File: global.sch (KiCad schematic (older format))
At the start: 37 parts, among them Q5 MMBT3904, U11 74HC165, U12 74HC595, U13 74HC595, U14 74HC595, U5 74HCT125

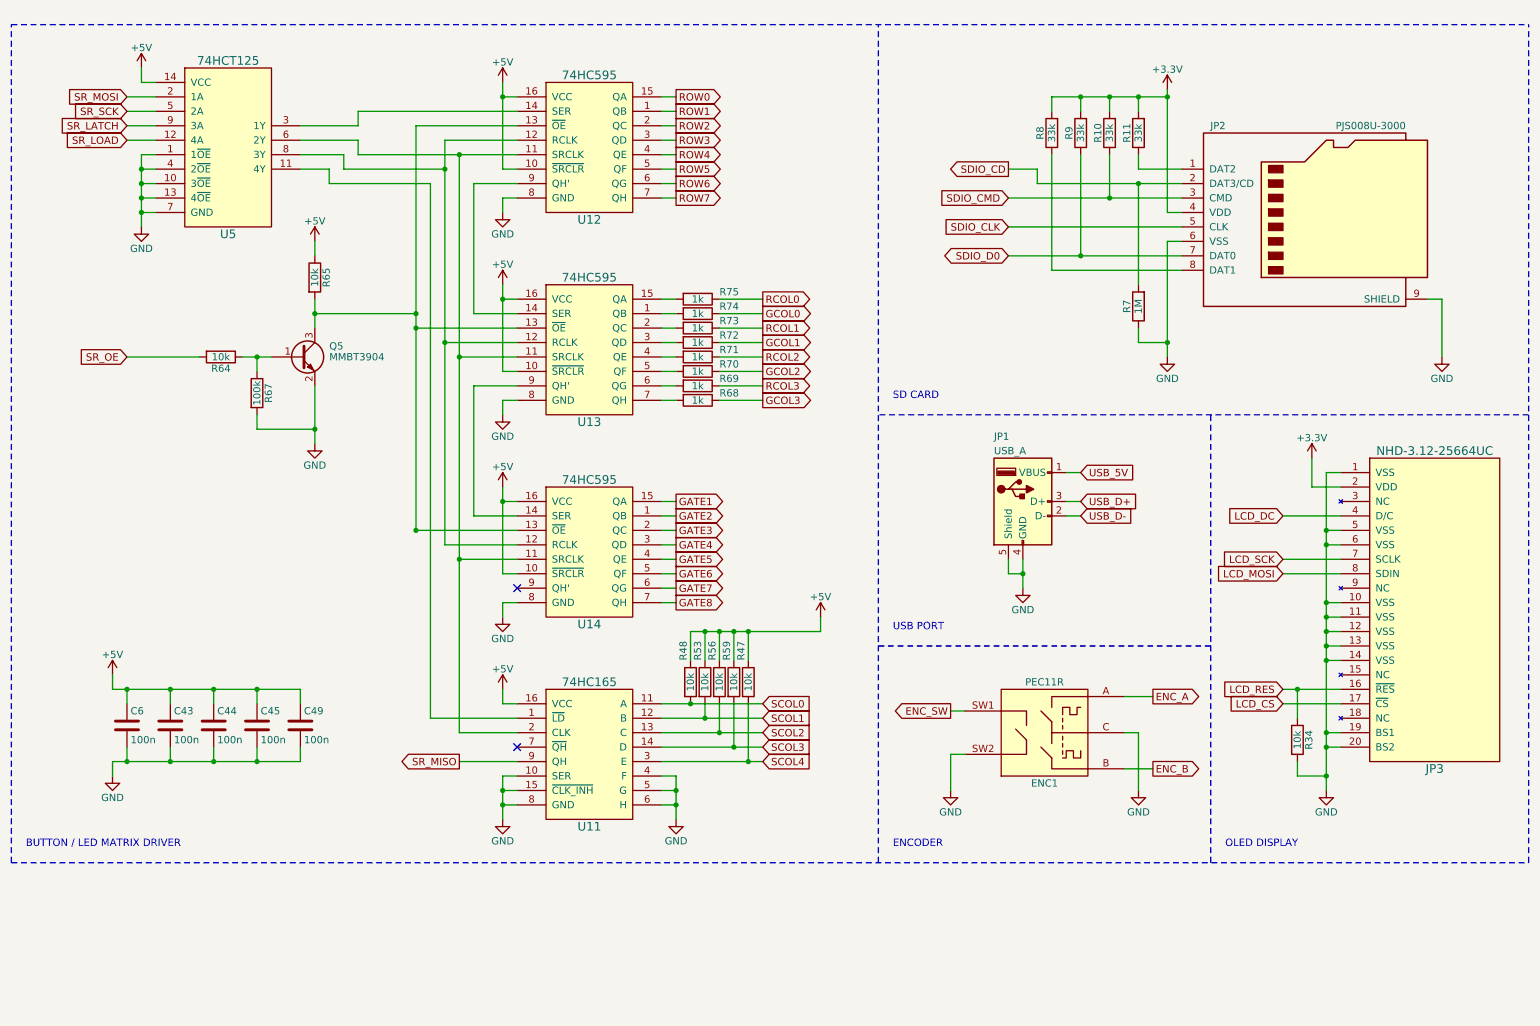
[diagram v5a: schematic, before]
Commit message: revised schematic and pcb
- fixed clock/reset inputs
- schematic annotations
- moved to cc-by-nc-sa
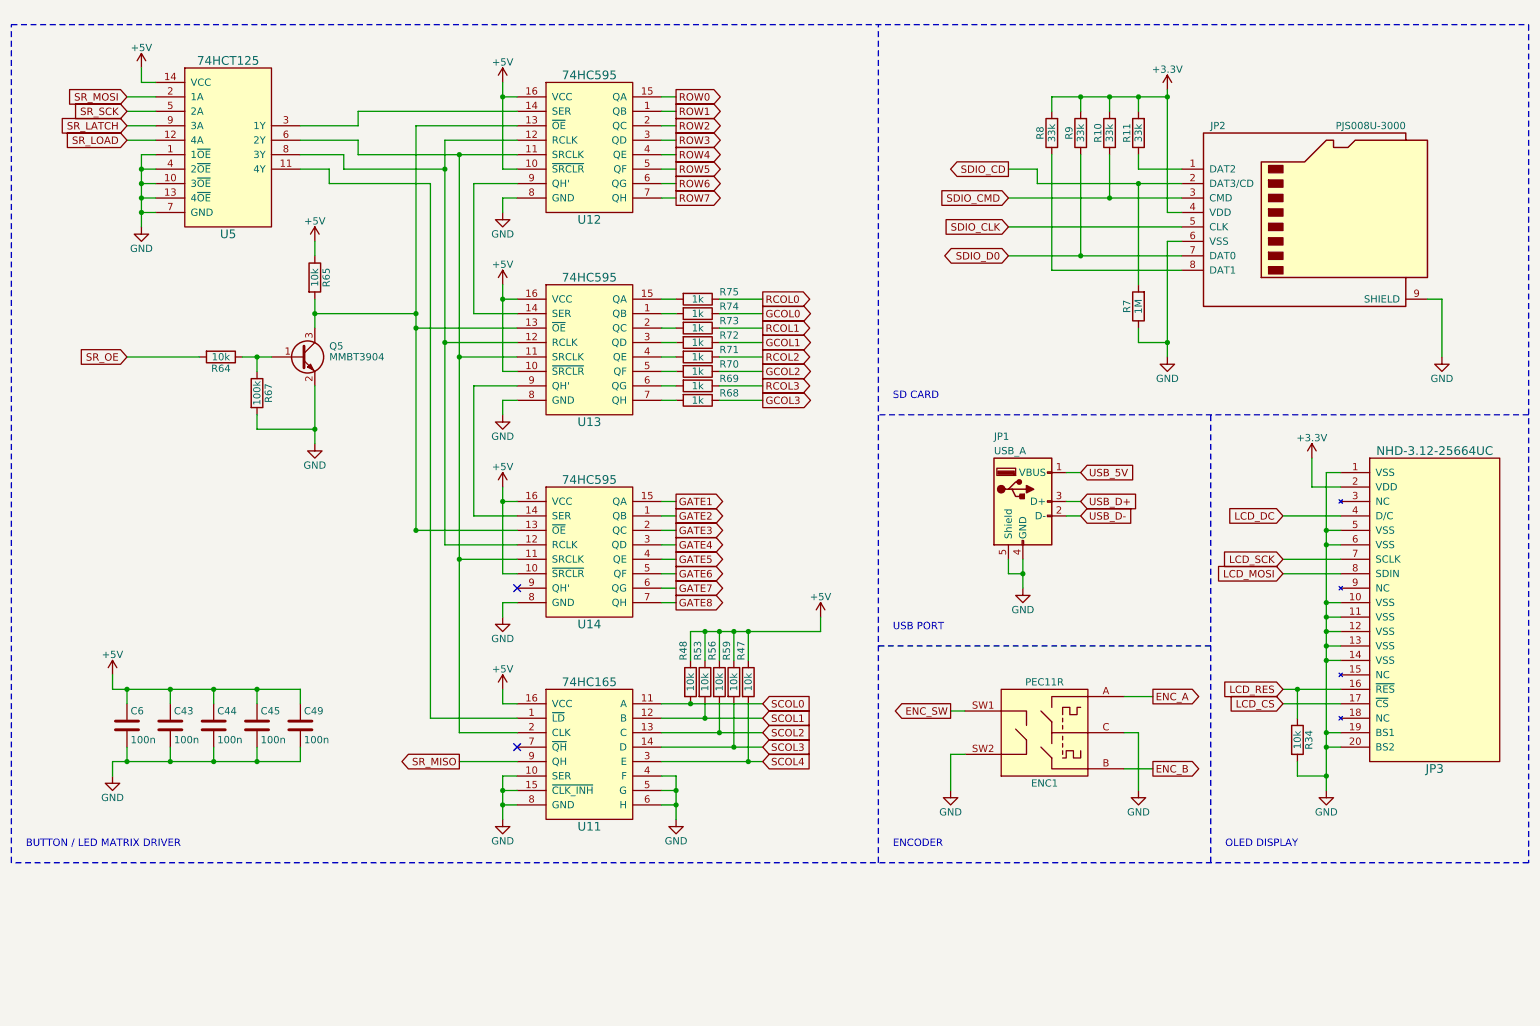
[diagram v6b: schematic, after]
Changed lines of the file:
@@
 Text GLabel 1400 2900 0    51   Input ~ 0
 SR_OE
+Text Notes 700  6300 0    51   ~ 0
+BUTTON / LED MATRIX DRIVER
+Text Notes 6700 3200 0    51   ~ 0
+SD CARD
+Text Notes 9000 6300 0    51   ~ 0
+OLED DISPLAY
+Text Notes 6700 6300 0    51   ~ 0
+ENCODER
+Text Notes 6700 4800 0    51   ~ 0
+USB PORT
 Wire Wire Line
 	5100 1100 5200 1100
@@
 Wire Wire Line
 	2300 3400 2700 3400
+Wire Notes Line
+	600  600  11100 600
+Wire Notes Line
+	11100 600  11100 6400
+Wire Notes Line
+	11100 3300 6600 3300
+Wire Notes Line
+	11100 6400 600  6400
+Wire Notes Line
+	8900 6400 8900 3300
+Wire Notes Line
+	8900 4900 6600 4900
+Wire Notes Line
+	6600 6400 6600 600
+Wire Notes Line
+	600  6400 600  600
 Connection ~ 4000 3900
 Connection ~ 4000 2500
@@
 NoConn ~ 4100 5600
 NoConn ~ 4100 4500
-Wire Notes Line
-	600  600  11100 600
-Text Notes 700  6300 0    51   ~ 0
-BUTTON / LED MATRIX DRIVER
-Wire Notes Line
-	11100 6400 11100 600
-Wire Notes Line
-	11100 3300 6600 3300
-Text Notes 6700 3200 0    51   ~ 0
-SD CARD
-Wire Notes Line
-	600  6400 11100 6400
-Wire Notes Line
-	8900 6400 8900 3300
-Text Notes 9000 6300 0    51   ~ 0
-OLED DISPLAY
-Text Notes 6700 6300 0    51   ~ 0
-ENCODER
-Wire Notes Line
-	8900 4900 6600 4900
-Text Notes 6700 4800 0    51   ~ 0
-USB PORT
-Wire Notes Line
-	6600 6400 6600 600
-Wire Notes Line
-	600  6400 600  600
 $EndSCHEMATC

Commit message: renumbered components
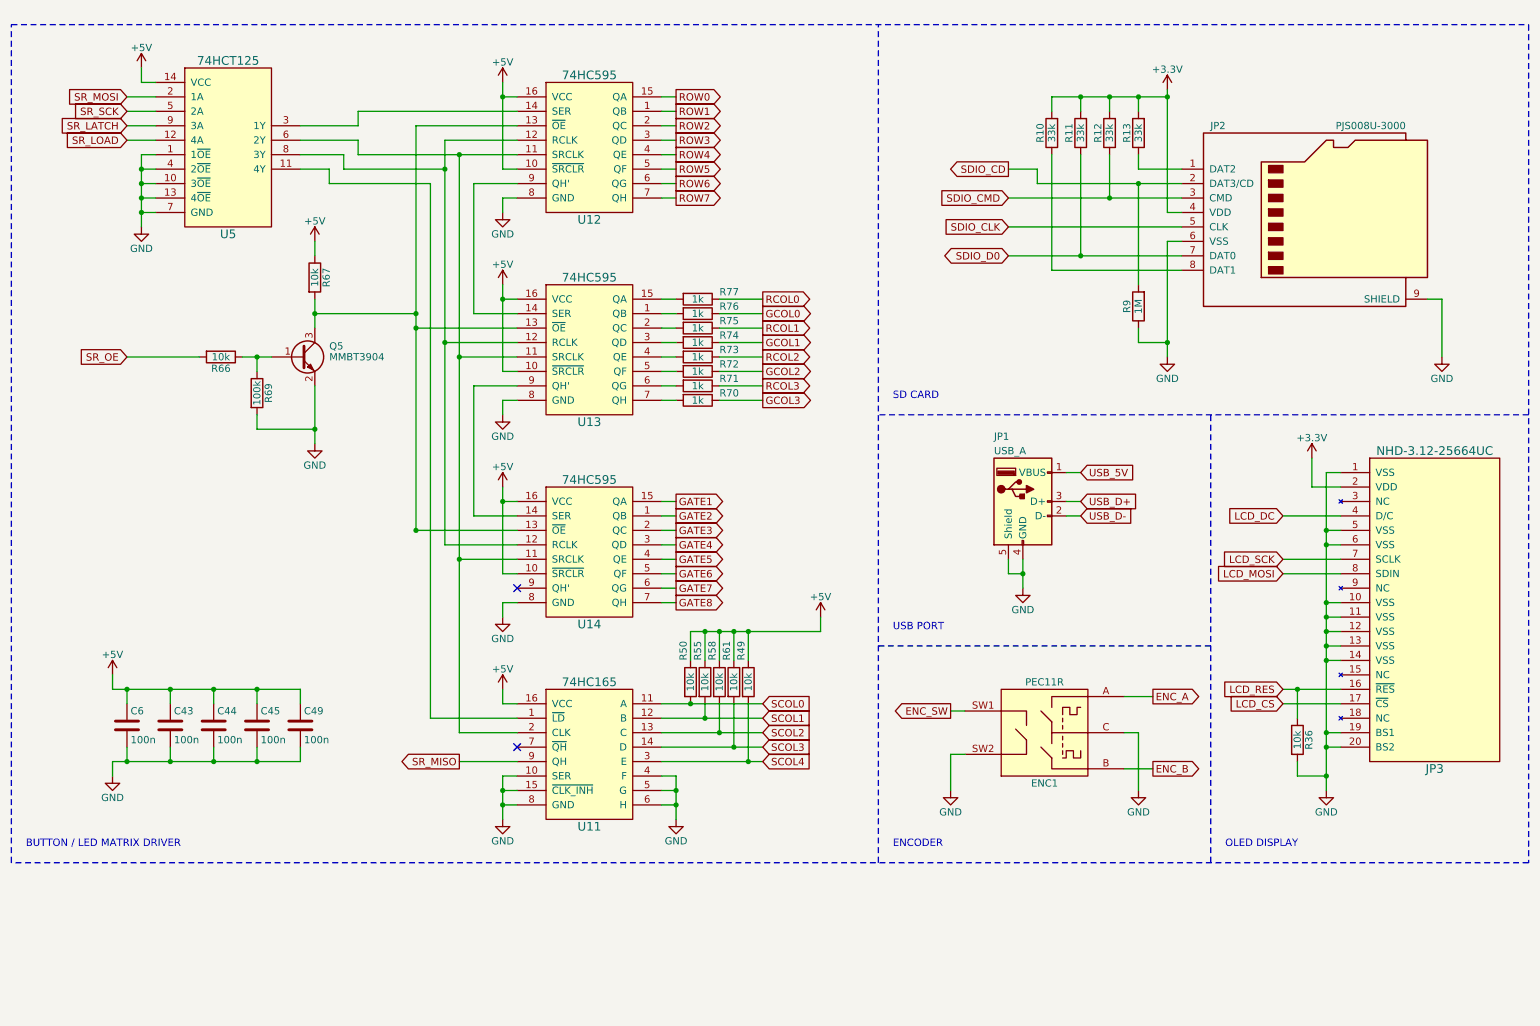
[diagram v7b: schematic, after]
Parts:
- renumbered R8 to R10, R9 to R11, R10 to R12, R11 to R13, R34 to R36, R47 to R49, R48 to R50, R53 to R55, R56 to R58, R59 to R61, R64 to R66, R65 to R67, R67 to R69, R68 to R70, R69 to R71, R70 to R72, R71 to R73, R72 to R74, R73 to R75, R74 to R76, R75 to R77, R7 to R9
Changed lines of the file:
@@
 $EndComp
 $Comp
-L R R48
+L R R50
 U 1 1 59E55F0E
 P 5300 5150
-F 0 "R48" V 5250 5300 50  0000 L CNN
+F 0 "R50" V 5250 5300 50  0000 L CNN
 F 1 "10k" V 5300 5150 50  0000 C CNN
 F 2 "w_resistor:R_0603" V 5230 5150 50  0001 C CNN
@@
 $EndComp
 $Comp
-L R R53
+L R R55
 U 1 1 59E560D3
 P 5400 5150
-F 0 "R53" V 5350 5300 50  0000 L CNN
+F 0 "R55" V 5350 5300 50  0000 L CNN
 F 1 "10k" V 5400 5150 50  0000 C CNN
 F 2 "w_resistor:R_0603" V 5330 5150 50  0001 C CNN
@@
 $EndComp
 $Comp
-L R R56
+L R R58
 U 1 1 59E56118
 P 5500 5150
-F 0 "R56" V 5450 5300 50  0000 L CNN
+F 0 "R58" V 5450 5300 50  0000 L CNN
 F 1 "10k" V 5500 5150 50  0000 C CNN
 F 2 "w_resistor:R_0603" V 5430 5150 50  0001 C CNN
@@
 $EndComp
 $Comp
-L R R59
+L R R61
 U 1 1 59E56160
 P 5600 5150
-F 0 "R59" V 5550 5300 50  0000 L CNN
+F 0 "R61" V 5550 5300 50  0000 L CNN
 F 1 "10k" V 5600 5150 50  0000 C CNN
 F 2 "w_resistor:R_0603" V 5530 5150 50  0001 C CNN
@@
 $EndComp
 $Comp
-L R R47
+L R R49
 U 1 1 59E561AB
 P 5700 5150
-F 0 "R47" V 5650 5300 50  0000 L CNN
+F 0 "R49" V 5650 5300 50  0000 L CNN
 F 1 "10k" V 5700 5150 50  0000 C CNN
 F 2 "w_resistor:R_0603" V 5630 5150 50  0001 C CNN
@@
 $EndComp
 $Comp
-L R R74
+L R R76
 U 1 1 59E604C8
 P 5350 2600
-F 0 "R74" V 5300 2750 50  0000 L CNN
+F 0 "R76" V 5300 2750 50  0000 L CNN
 F 1 "1k" V 5350 2600 50  0000 C CNN
 F 2 "w_resistor:R_0603" V 5280 2600 50  0001 C CNN
@@
 $EndComp
 $Comp
-L R R75
+L R R77
 U 1 1 59E60528
 P 5350 2500
-F 0 "R75" V 5300 2650 50  0000 L CNN
+F 0 "R77" V 5300 2650 50  0000 L CNN
 F 1 "1k" V 5350 2500 50  0000 C CNN
 F 2 "w_resistor:R_0603" V 5280 2500 50  0001 C CNN
@@
 $EndComp
 $Comp
-L R R73
+L R R75
 U 1 1 59E60C94
 P 5350 2700
-F 0 "R73" V 5300 2850 50  0000 L CNN
+F 0 "R75" V 5300 2850 50  0000 L CNN
 F 1 "1k" V 5350 2700 50  0000 C CNN
 F 2 "w_resistor:R_0603" V 5280 2700 50  0001 C CNN
@@
 $EndComp
 $Comp
-L R R72
+L R R74
 U 1 1 59E60F5A
 P 5350 2800
-F 0 "R72" V 5300 2950 50  0000 L CNN
+F 0 "R74" V 5300 2950 50  0000 L CNN
 F 1 "1k" V 5350 2800 50  0000 C CNN
 F 2 "w_resistor:R_0603" V 5280 2800 50  0001 C CNN
@@
 $EndComp
 $Comp
-L R R68
+L R R70
 U 1 1 59E61471
 P 5350 3200
-F 0 "R68" V 5300 3350 50  0000 L CNN
+F 0 "R70" V 5300 3350 50  0000 L CNN
 F 1 "1k" V 5350 3200 50  0000 C CNN
 F 2 "w_resistor:R_0603" V 5280 3200 50  0001 C CNN
@@
 $EndComp
 $Comp
-L R R69
+L R R71
 U 1 1 59E6153A
 P 5350 3100
-F 0 "R69" V 5300 3250 50  0000 L CNN
+F 0 "R71" V 5300 3250 50  0000 L CNN
 F 1 "1k" V 5350 3100 50  0000 C CNN
 F 2 "w_resistor:R_0603" V 5280 3100 50  0001 C CNN
@@
 $EndComp
 $Comp
-L R R70
+L R R72
 U 1 1 59E61584
 P 5350 3000
-F 0 "R70" V 5300 3150 50  0000 L CNN
+F 0 "R72" V 5300 3150 50  0000 L CNN
 F 1 "1k" V 5350 3000 50  0000 C CNN
 F 2 "w_resistor:R_0603" V 5280 3000 50  0001 C CNN
@@
 $EndComp
 $Comp
-L R R71
+L R R73
 U 1 1 59E6158A
 P 5350 2900
-F 0 "R71" V 5300 3050 50  0000 L CNN
+F 0 "R73" V 5300 3050 50  0000 L CNN
 F 1 "1k" V 5350 2900 50  0000 C CNN
 F 2 "w_resistor:R_0603" V 5280 2900 50  0001 C CNN
@@
 $EndComp
 $Comp
-L R R11
+L R R13
 U 1 1 5AEA4C2A
 P 8400 1350
-F 0 "R11" V 8480 1350 50  0000 C CNN
+F 0 "R13" V 8480 1350 50  0000 C CNN
 F 1 "33k" V 8400 1350 50  0000 C CNN
 F 2 "w_resistor:R_0603" V 8330 1350 50  0001 C CNN
@@
 $EndComp
 $Comp
-L R R7
+L R R9
 U 1 1 5AEA4CDA
 P 8400 2550
-F 0 "R7" V 8480 2550 50  0000 C CNN
+F 0 "R9" V 8480 2550 50  0000 C CNN
 F 1 "1M" V 8400 2550 50  0000 C CNN
 F 2 "w_resistor:R_0603" V 8330 2550 50  0001 C CNN
@@
 $EndComp
 $Comp
-L R R8
+L R R10
 U 1 1 5AEA4D5E
 P 7800 1350
-F 0 "R8" V 7880 1350 50  0000 C CNN
+F 0 "R10" V 7880 1350 50  0000 C CNN
 F 1 "33k" V 7800 1350 50  0000 C CNN
 F 2 "w_resistor:R_0603" V 7730 1350 50  0001 C CNN
@@
 $EndComp
 $Comp
-L R R9
+L R R11
 U 1 1 5AEA4DC8
 P 8000 1350
-F 0 "R9" V 8080 1350 50  0000 C CNN
+F 0 "R11" V 8080 1350 50  0000 C CNN
 F 1 "33k" V 8000 1350 50  0000 C CNN
 F 2 "w_resistor:R_0603" V 7930 1350 50  0001 C CNN
@@
 $EndComp
 $Comp
-L R R10
+L R R12
 U 1 1 5AEA93F2
 P 8200 1350
-F 0 "R10" V 8280 1350 50  0000 C CNN
+F 0 "R12" V 8280 1350 50  0000 C CNN
 F 1 "33k" V 8200 1350 50  0000 C CNN
 F 2 "w_resistor:R_0603" V 8130 1350 50  0001 C CNN
@@
 $EndComp
 $Comp
-L R R34
+L R R36
 U 1 1 5AEB2AD1
 P 9500 5550
-F 0 "R34" V 9580 5550 50  0000 C CNN
+F 0 "R36" V 9580 5550 50  0000 C CNN
 F 1 "10k" V 9500 5550 50  0000 C CNN
 F 2 "w_resistor:R_0603" V 9430 5550 50  0001 C CNN
@@
 $EndComp
 $Comp
-L R R65
+L R R67
 U 1 1 5AEB9A79
 P 2700 2350
-F 0 "R65" V 2780 2350 50  0000 C CNN
+F 0 "R67" V 2780 2350 50  0000 C CNN
 F 1 "10k" V 2700 2350 50  0000 C CNN
 F 2 "w_resistor:R_0603" V 2630 2350 50  0001 C CNN
@@
 $EndComp
 $Comp
-L R R64
+L R R66
 U 1 1 5AEBCC66
 P 2050 2900
-F 0 "R64" V 2130 2900 50  0000 C CNN
+F 0 "R66" V 2130 2900 50  0000 C CNN
 F 1 "10k" V 2050 2900 50  0000 C CNN
 F 2 "w_resistor:R_0603" V 1980 2900 50  0001 C CNN
@@
 $EndComp
 $Comp
-L R R67
+L R R69
 U 1 1 5AEBCE61
 P 2300 3150
-F 0 "R67" V 2380 3150 50  0000 C CNN
+F 0 "R69" V 2380 3150 50  0000 C CNN
 F 1 "100k" V 2300 3150 50  0000 C CNN
 F 2 "w_resistor:R_0603" V 2230 3150 50  0001 C CNN
